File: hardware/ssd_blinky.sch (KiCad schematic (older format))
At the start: 0 parts

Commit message: incremental progress on schematic
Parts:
- added C?: C, symbol C
- added CON?: AVR-ISP-6, AVR-ISP-6, symbol AVR-ISP-6
- added IC?: ATTINY25-S, SO8-200, symbol ATTINY25-S
- added R? (x3): R, symbol R
- added SW?: SW_PUSH, symbol SW_PUSH
- added U?: ASMT-YTC2-0AA02, symbol ASMT-YTC2-0AA02
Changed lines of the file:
@@
-EESchema Schematic File Version 2  date Sat 22 Feb 2014 08:26:49 PM MST
+EESchema Schematic File Version 2
 LIBS:power
 LIBS:device
@@
 LIBS:contrib
 LIBS:valves
-EELAYER 43  0
+EELAYER 24 0
 EELAYER END
-$Descr A4 11700 8267
+$Descr A4 11693 8268
 encoding utf-8
 Sheet 1 1
@@
 Comment4 ""
 $EndDescr
+$Comp
+L ATTINY25-S IC?
+U 1 1 53097DB5
+P 5100 3500
+F 0 "IC?" H 3950 3900 40  0000 C CNN
+F 1 "ATTINY25-S" H 6100 3100 40  0000 C CNN
+F 2 "SO8-200" H 6050 3500 35  0000 C CIN
+F 3 "" H 5100 3500 60  0000 C CNN
+	1    5100 3500
+	1    0    0    -1
+$EndComp
+$Comp
+L AVR-ISP-6 CON?
+U 1 1 53097DCE
+P 8000 3600
+F 0 "CON?" H 7920 3840 50  0000 C CNN
+F 1 "AVR-ISP-6" H 7760 3370 50  0000 L BNN
+F 2 "AVR-ISP-6" V 7480 3640 50  0001 C CNN
+F 3 "" H 8000 3600 60  0000 C CNN
+	1    8000 3600
+	1    0    0    -1
+$EndComp
+$Comp
+L ASMT-YTC2-0AA02 U?
+U 1 1 53097E00
+P 7400 4350
+F 0 "U?" H 7400 4650 60  0000 C CNN
+F 1 "ASMT-YTC2-0AA02" H 7350 4050 60  0000 C CNN
+F 2 "" H 7400 4350 60  0000 C CNN
+F 3 "" H 7400 4350 60  0000 C CNN
+	1    7400 4350
+	1    0    0    -1
+$EndComp
+$Comp
+L R R?
+U 1 1 53097F70
+P 6550 5400
+F 0 "R?" V 6630 5400 40  0000 C CNN
+F 1 "R" V 6557 5401 40  0000 C CNN
+F 2 "" V 6480 5400 30  0000 C CNN
+F 3 "" H 6550 5400 30  0000 C CNN
+	1    6550 5400
+	1    0    0    -1
+$EndComp
+$Comp
+L R R?
+U 1 1 53097F84
+P 6850 5400
+F 0 "R?" V 6930 5400 40  0000 C CNN
+F 1 "R" V 6857 5401 40  0000 C CNN
+F 2 "" V 6780 5400 30  0000 C CNN
+F 3 "" H 6850 5400 30  0000 C CNN
+	1    6850 5400
+	1    0    0    -1
+$EndComp
+$Comp
+L R R?
+U 1 1 53097F98
+P 7200 5400
+F 0 "R?" V 7280 5400 40  0000 C CNN
+F 1 "R" V 7207 5401 40  0000 C CNN
+F 2 "" V 7130 5400 30  0000 C CNN
+F 3 "" H 7200 5400 30  0000 C CNN
+	1    7200 5400
+	1    0    0    -1
+$EndComp
+$Comp
+L C C?
+U 1 1 53097FAC
+P 5650 4400
+F 0 "C?" H 5650 4500 40  0000 L CNN
+F 1 "C" H 5656 4315 40  0000 L CNN
+F 2 "" H 5688 4250 30  0000 C CNN
+F 3 "" H 5650 4400 60  0000 C CNN
+	1    5650 4400
+	1    0    0    -1
+$EndComp
+$Comp
+L SW_PUSH SW?
+U 1 1 53097FC0
+P 4200 2700
+F 0 "SW?" H 4350 2810 50  0000 C CNN
+F 1 "SW_PUSH" H 4200 2620 50  0000 C CNN
+F 2 "" H 4200 2700 60  0000 C CNN
+F 3 "" H 4200 2700 60  0000 C CNN
+	1    4200 2700
+	1    0    0    -1
+$EndComp
 $EndSCHEMATC

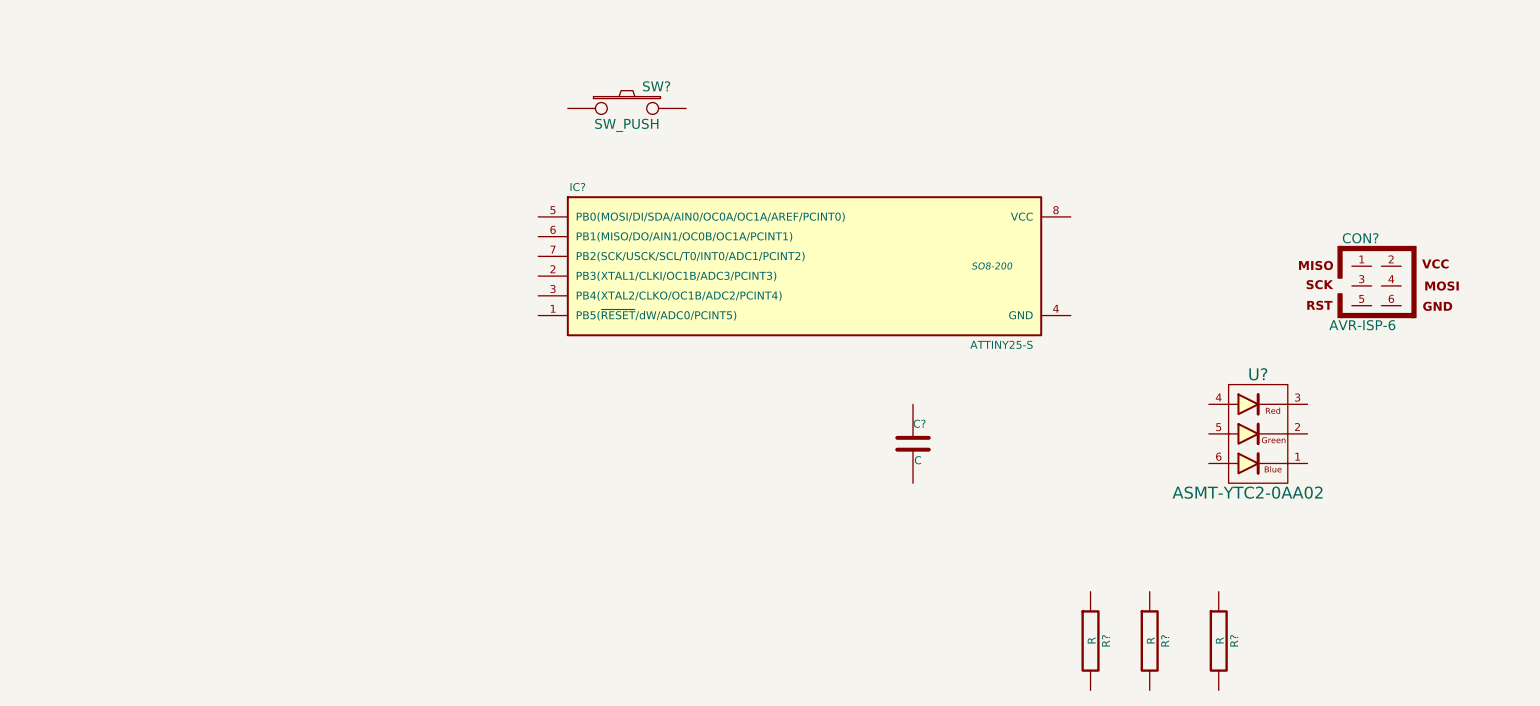
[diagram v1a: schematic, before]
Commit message: added orblink reference design files, component value calculation spreadsheet, and updated kicad design files
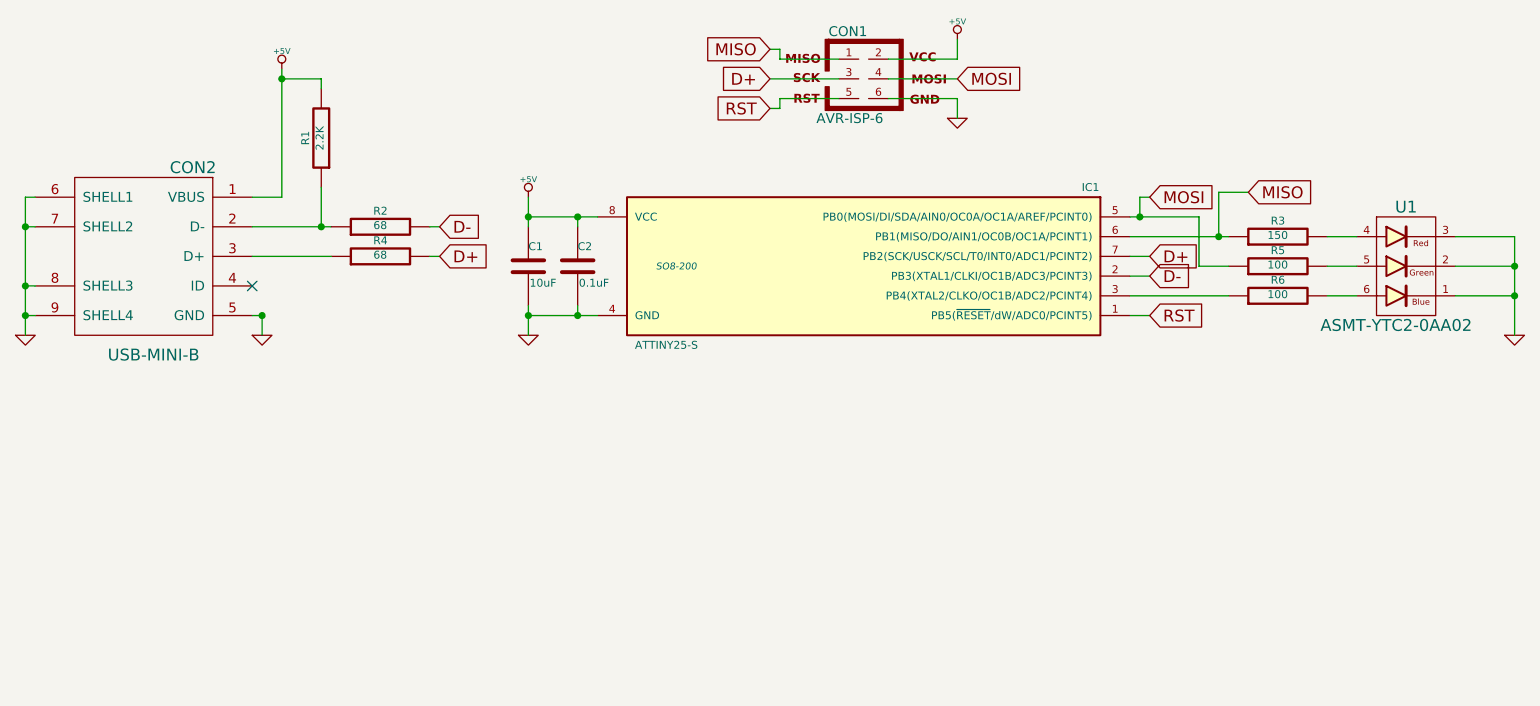
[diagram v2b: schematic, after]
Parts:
- removed SW?: SW_PUSH, symbol SW_PUSH
- added C1: 10uF, symbol C
- added CON2: USB-MINI-B, symbol USB-MINI-B
- added R1: 2.2K, symbol R
- added R2, R4: 68, symbol R
- C2: renamed from C?; value C -> 0.1uF
- R3: renamed from R?; value R -> 150
- R5, R6: renamed from R?; value R -> 100
- gave numbers to parts that had none: 3
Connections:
- net RST: now reaches IC1.1 (PB5(~RESET~/dW/ADC0/PCINT5))
- net RST: now also CON1.5
- net D-: now reaches IC1.2 (PB3(XTAL1/CLKI/OC1B/ADC3/PCINT3))
- net D-: now also R2.2
- net at IC1.3 (PB4(XTAL2/CLKO/OC1B/ADC2/PCINT4)): now also R6.1
- net GND: now reaches IC1.4 (GND)
- net GND: now also C2.2, CON1.6, U1.1 (KB), U1.2 (KG), U1.3 (KR), C1.2, CON2.5 (GND), CON2.6 (SHELL1), CON2.7 (SHELL2), CON2.8 (SHELL3), CON2.9 (SHELL4)
- net MOSI: now reaches IC1.5 (PB0(MOSI/DI/SDA/AIN0/OC0A/OC1A/AREF/PCINT0))
- net MOSI: now also CON1.4, R5.1
- net MISO: now reaches IC1.6 (PB1(MISO/DO/AIN1/OC0B/OC1A/PCINT1))
- net MISO: now also CON1.1, R3.1
- net D+: now reaches IC1.7 (PB2(SCK/USCK/SCL/T0/INT0/ADC1/PCINT2))
- net D+: now also CON1.3, R4.2
- net +5V: now reaches IC1.8 (VCC)
- net +5V: now also C2.1, CON1.2, C1.1, CON2.1 (VBUS), R1.2
- net at U1.4 (AR): now also R3.2
- net at U1.5 (AG): now also R5.2
- net at U1.6 (AB): now also R6.2
- new net: CON2.2 (D-), R1.1, R2.1
- new net: CON2.3 (D+), R4.1
- no-connect marks 0 -> 1
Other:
- moved on the sheet: C2, CON1, IC1, R3, R5, R6, U1
